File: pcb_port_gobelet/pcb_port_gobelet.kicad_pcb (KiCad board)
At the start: 2 copper layers, 25.8 x 25 mm, 5 parts

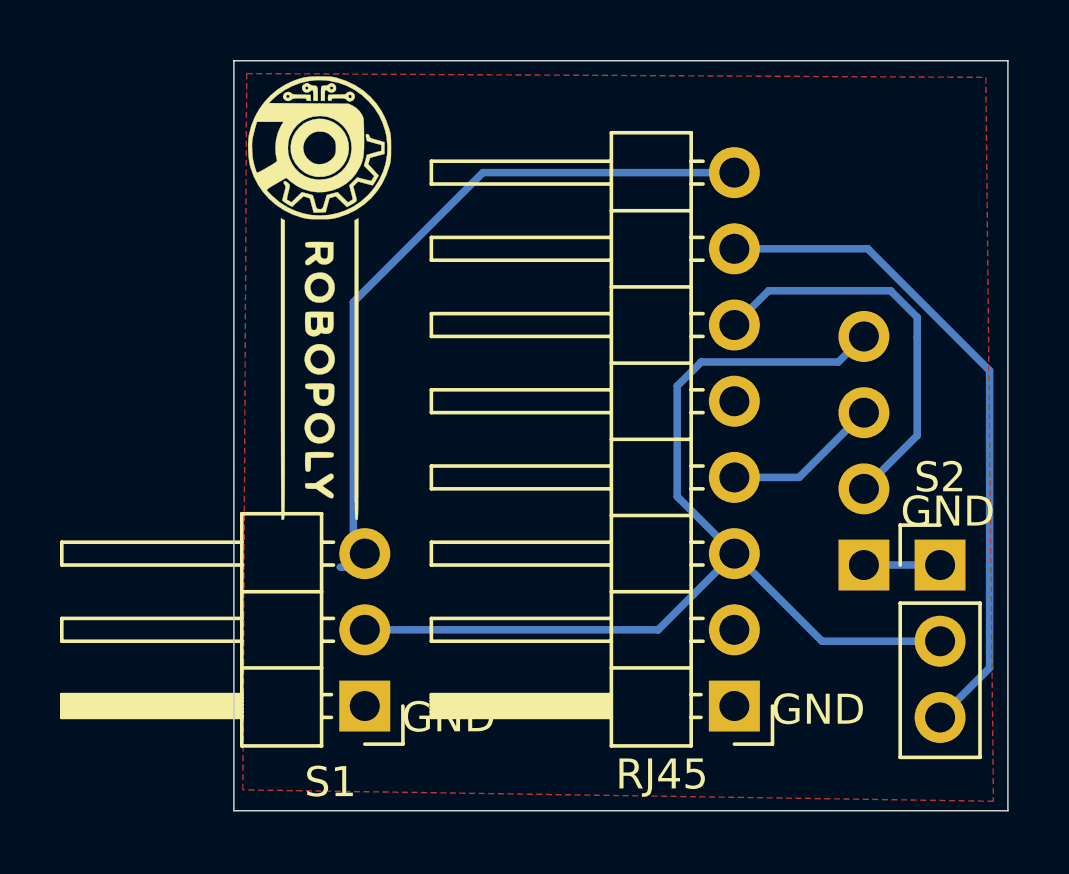
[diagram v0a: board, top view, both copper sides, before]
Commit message: Update PCB after v1
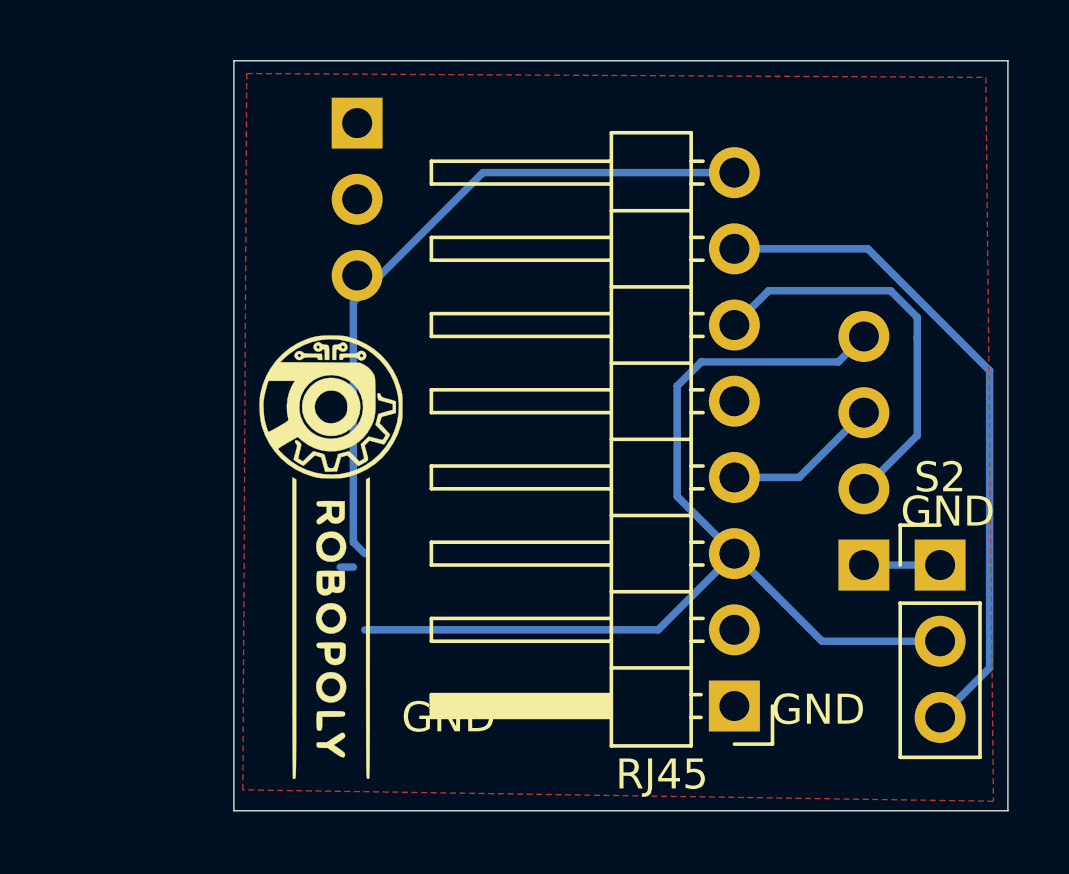
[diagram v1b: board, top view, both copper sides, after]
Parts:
- S1: moved to B.Cu
- moved S1 19.4 mm to (122.8, 116.1)
- moved REF** 8.64 mm to (122.0, 131.4)
